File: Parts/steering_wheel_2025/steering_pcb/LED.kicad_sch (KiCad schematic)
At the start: 3 parts, among them J13 PINHD_1x1_Male, Q4 BS170

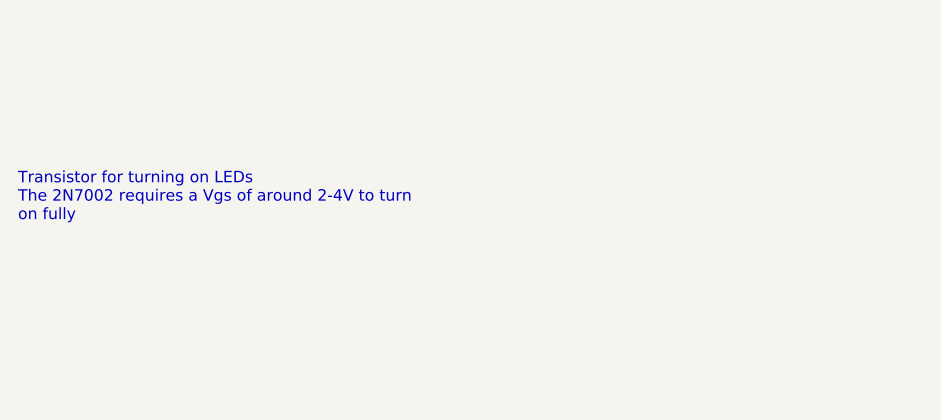
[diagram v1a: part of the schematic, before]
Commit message: slight changes in schematic
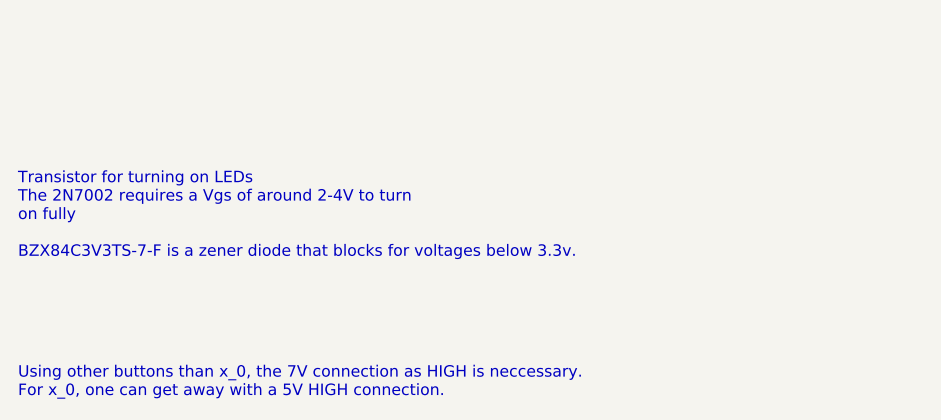
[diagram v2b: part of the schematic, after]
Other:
- note added: "Transistor for turning on LEDs The 2N7002 requires a Vgs of around 2-4V to turn on fully BZX84C3V3TS-7-F is a zener diode that blocks for voltages below 3.3v."
- note added: "Using other buttons than x_0, the 7V connection as HIGH is neccessary. For x_0, one can get away with a 5V HIGH connection."
- note removed: "Transistor for turning on LEDs The 2N7002 requires a Vgs of around 2-4V to turn on fully"
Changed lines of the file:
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@@
 		)
 	)
-	(text "Transistor for turning on LEDs\nThe 2N7002 requires a Vgs of around 2-4V to turn\non fully"
+	(text "Transistor for turning on LEDs\nThe 2N7002 requires a Vgs of around 2-4V to turn\non fully\n\nBZX84C3V3TS-7-F is a zener diode that blocks for voltages below 3.3v.\n"
 		(exclude_from_sim no)
-		(at 14.478 122.936 0)
+		(at 14.478 120.142 0)
 		(effects
 			(font
+				(size 1.27 1.27)
+			)
+			(justify left top)
+		)
+	)
+	(text "Using other buttons than x_0, the 7V connection as HIGH is neccessary.\nFor x_0, one can get away with a 5V HIGH connection."
+		(exclude_from_sim no)
+		(at 14.478 143.51 0)
+		(effects
+			(font

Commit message: Dashboard electron
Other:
- moved on the sheet: J13, JP8, Q4
